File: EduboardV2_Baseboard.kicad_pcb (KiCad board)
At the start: 2 copper layers, 100 x 160 mm, 145 parts, among them IC201 STK8321, IC202 PCF8563T_5,518, IC203 W25Q128JVSIQTR, IC301 XL1509-5.0E1, IC302 SY8113BADC, IC601 STK8321, IC602 SP3485EN-L_TR, IC603 WM8782SEDS_RV_C323842, IC604 CS4344-CZZ, IC605 MCP9700AT-E_TT, SW301 1FS1T1B9M2RES-5, SW401 K2-1102SP-C4SC-04, SW402 K2-1102SP-C4SC-04, SW403 K2-1102SP-C4SC-04, SW404 K2-1102SP-C4SC-04, T401 AO3400A, T402 AO3400A, T403 AO3400A, T404 AO3400A, T405 AO3400A, X201 PCIE-52P40H, X202 32.768 kHz, X203 TF-15×15, X204 CR1220-2ZX, X301 KF2EDGR-3.81-3P, X302 USB3.1C16PFSMT, X303 CH340G, X401 ER-TFT035-6, X501 BH-00105, X502 S4B-PH-SM4-K-TB(LF)(SN), X503 USB3.1C16PFSMT, X601 KF2EDGR-3.81-3P, X602 PJ-327C-4A, X603 PJ-327C-4A, Y301 X322512MSB4SI

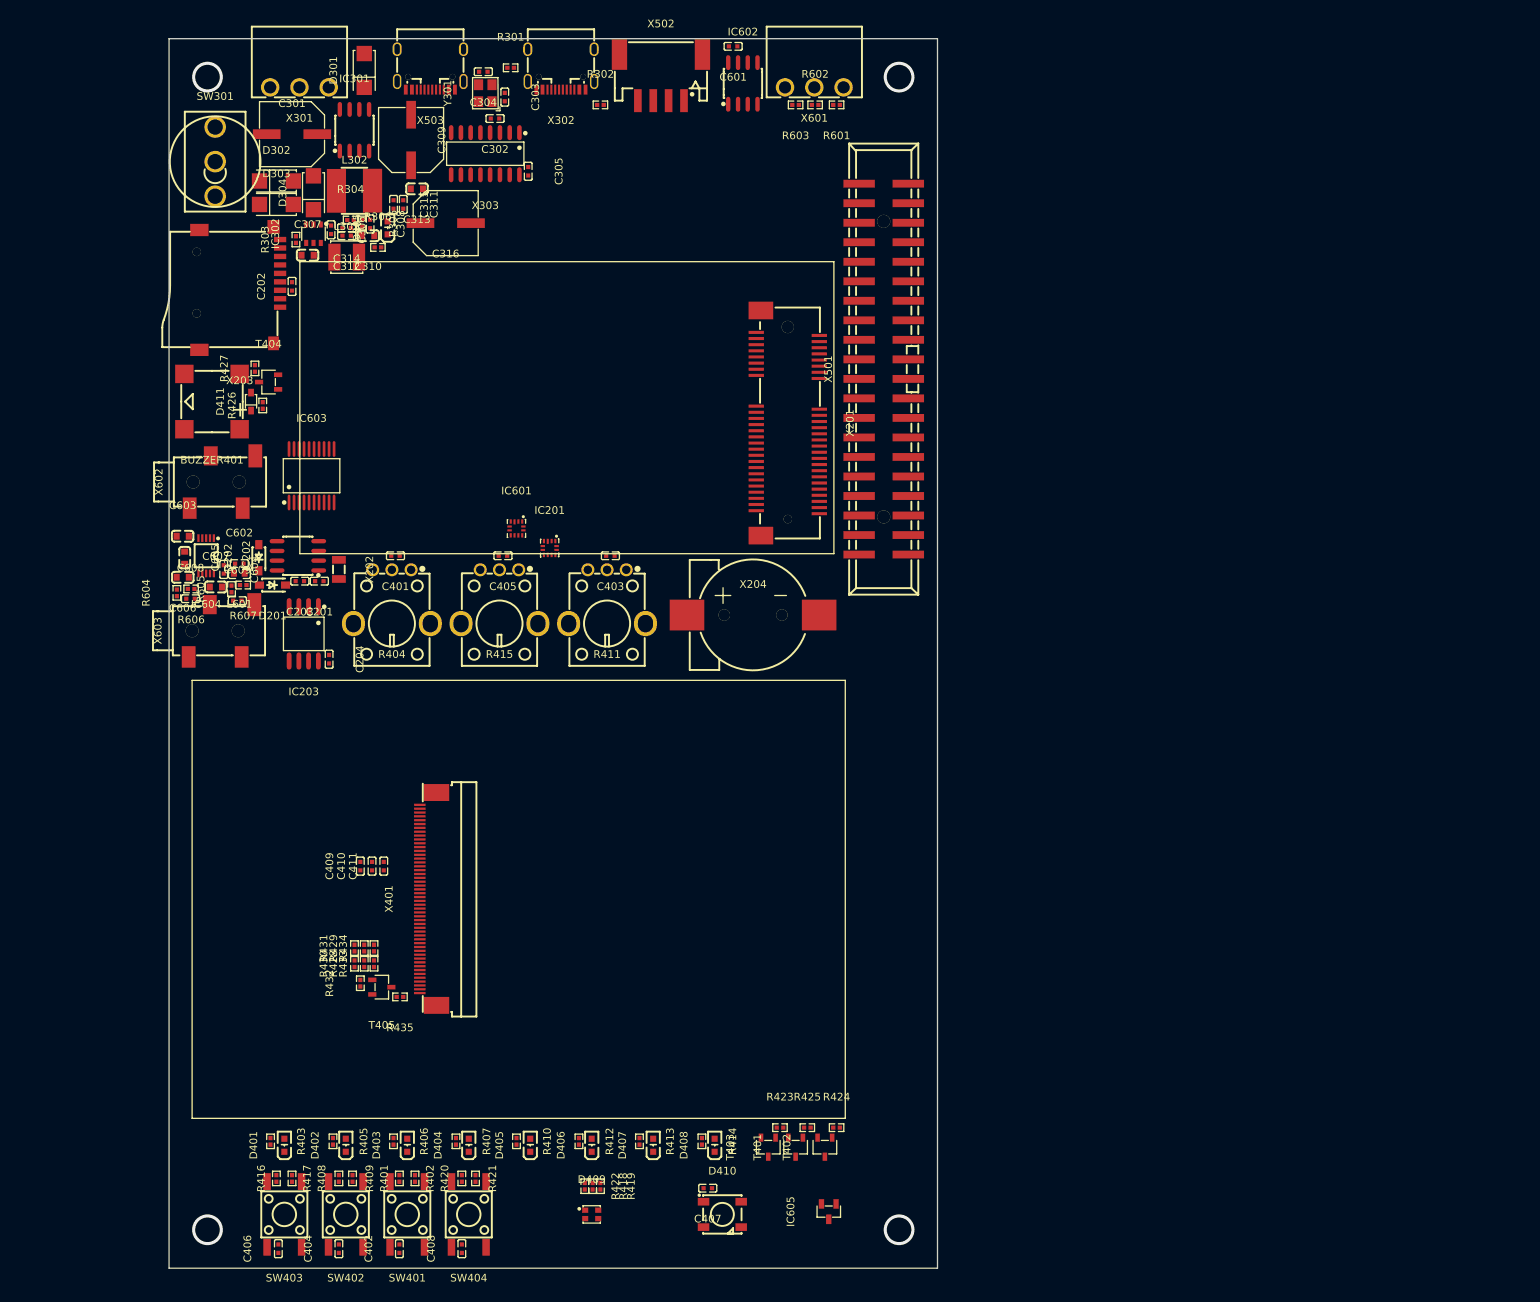
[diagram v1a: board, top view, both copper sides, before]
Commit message: reassign symbol references after page movements. Place in pcb
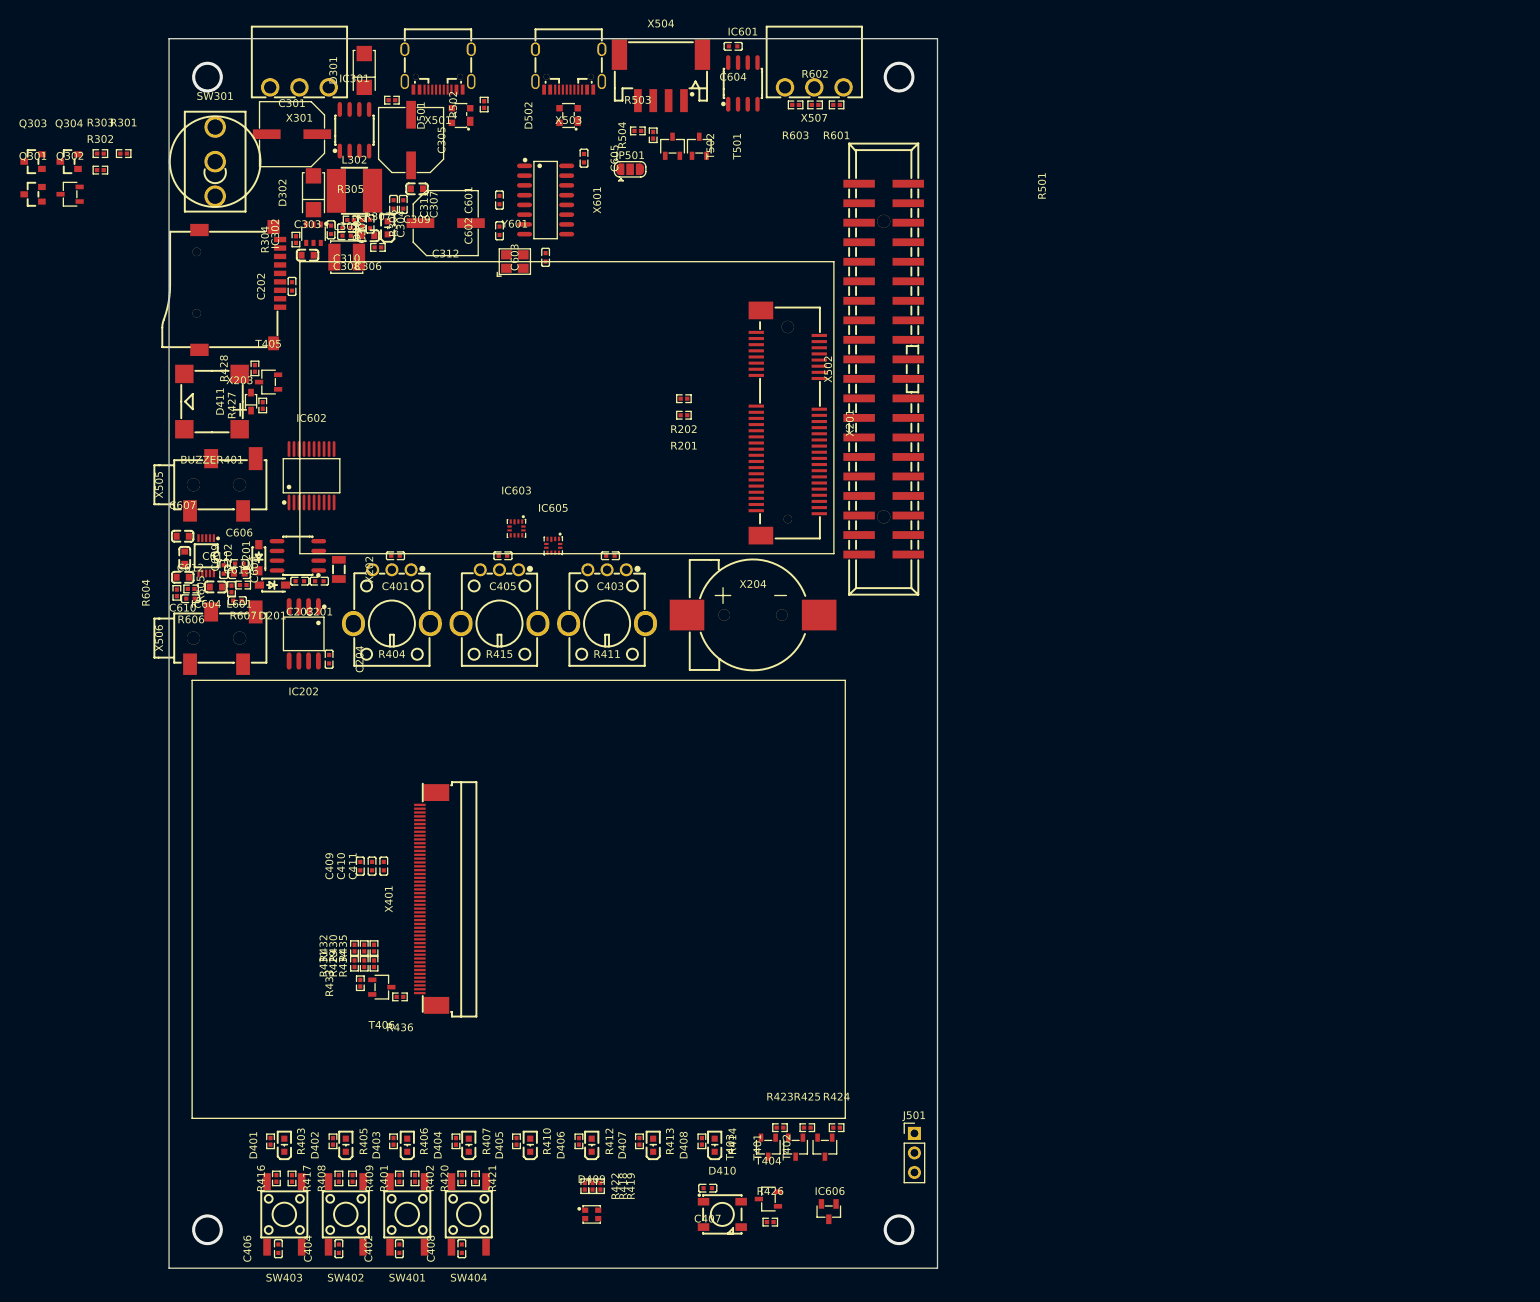
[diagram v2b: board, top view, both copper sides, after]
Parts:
- removed the C302 at (96.4, 31.4)
- removed the C303 at (97.7, 28.6)
- removed the C304 at (94.9, 25.3)
- removed the C305 at (100.7, 38.3)
- removed the D302 at (68.0, 39.5)
- removed the D303 at (68.0, 42.6)
- removed the IC201 at (103.5, 87.3)
- removed X302: USB3.1C16PFSMT, eduboardv2:USB-C-SMD_TYPE-C-USB-17
- removed X303: CH340G, eduboardv2:SOIC-16_L9.9-W3.9-P1.27-LS6.0-BL
- removed X602, X603: PJ-327C-4A, eduboardv2:AUDIO-SMD_PJ-327C-4A
- removed Y301: X322512MSB4SI, eduboardv2:OSC-SMD_4P-L3.2-W2.5-BL
- added C601: 100nF, 50V, eduboardv2:C0402, F.Cu at (97.0, 42.0)
- added C602: 22pF, eduboardv2:C0402, F.Cu at (97.0, 46.0)
- added C603: 22pF, eduboardv2:C0402, F.Cu at (103.0, 49.5)
- added C605: 100nF, 50V, eduboardv2:C0402, F.Cu at (108.0, 36.5)
- added D501: PRTR5V0U2X_C2827688, eduboardv2:SOT-143-4_L2.9-W1.3-P1.92-LS2.4-BL, F.Cu at (92.0, 31.0)
- added D502: PRTR5V0U2X_C2827688, eduboardv2:SOT-143-4_L2.9-W1.3-P1.92-LS2.4-BL, F.Cu at (106.0, 31.0)
- added IC605: STK8321, eduboardv2:LGA-12_L2.0-W2.0-P0.50-TR, F.Cu at (104.0, 87.0)
- added J501: Conn_WS2812_Extern, Connector_PinHeader_2.54mm:PinHeader_1x03_P2.54mm_Vertical, F.Cu at (151.0, 163.5)
- added JP501: Stemma Voltage Selector, Jumper:SolderJumper-3_P1.3mm_Open_RoundedPad1.0x1.5mm, F.Cu at (114.0, 38.0)
- added Q301: AO3401A, eduboardv2:SOT-23_L2.9-W1.3-P1.90-LS2.4-BR, F.Cu at (36.3, 41.2)
- added Q302: AO3400A, eduboardv2:SOT-23-3_L2.9-W1.6-P1.90-LS2.8-BR, F.Cu at (41.1, 41.2)
- added Q303: AO3401A, eduboardv2:SOT-23_L2.9-W1.3-P1.90-LS2.4-BR, F.Cu at (36.3, 37.0)
- added Q304: AO3401A, eduboardv2:SOT-23_L2.9-W1.3-P1.90-LS2.4-BR, F.Cu at (41.0, 37.0)
- added R201: 10k, eduboardv2:R0402, F.Cu at (121.0, 70.0)
- added R202: 10k, eduboardv2:R0402, F.Cu at (121.0, 67.8)
- added R303: 1M, eduboardv2:R0402, F.Cu at (45.1, 36.0)
- added R426: 10k, eduboardv2:R0402, F.Cu at (132.2, 175.0)
- added R501: 5.1k, eduboardv2:R0402, F.Cu at (83.0, 29.0)
- added R502: 5.1k, eduboardv2:R0402, F.Cu at (95.0, 29.6)
- added R503: 10k, eduboardv2:R0402, F.Cu at (115.0, 33.0)
- added R504: 10k, eduboardv2:R0402, F.Cu at (117.0, 33.6)
- added T404: AO3400A, eduboardv2:SOT-23-3_L2.9-W1.6-P1.90-LS2.8-BR, F.Cu at (132.0, 172.0)
- added T501: AO3400A, eduboardv2:SOT-23-3_L2.9-W1.6-P1.90-LS2.8-BR, F.Cu at (123.0, 35.0)
- added T502: AO3400A, eduboardv2:SOT-23-3_L2.9-W1.6-P1.90-LS2.8-BR, F.Cu at (119.5, 35.0)
- added X501: USB3.1C16PFSMT, eduboardv2:USB-C-SMD_TYPE-C-USB-17, F.Cu at (89.0, 25.0)
- added X505: PJ-327C-4A, eduboardv2:AUDIO-SMD_PJ-327C-4A, F.Cu at (61.0, 79.0)
- added X506: PJ-327C-4A, eduboardv2:AUDIO-SMD_PJ-327C-4A, F.Cu at (61.0, 99.0)
- added X507: KF2EDGR-3.81-3P, eduboardv2:CONN-TH_3P-P3.81_KF2EDGR-3.81-3P, F.Cu at (138.0, 27.3)
- added Y601: X322512MSB4SI, eduboardv2:OSC-SMD_4P-L3.2-W2.5-BL, F.Cu at (99.0, 50.0)
- R301, R302: value 5.1k -> 1M
- X601: value KF2EDGR-3.81-3P -> CH340G; footprint eduboardv2:CONN-TH_3P-P3.81_KF2EDGR-3.81-3P -> eduboardv2:SOIC-16_L9.9-W3.9-P1.27-LS6.0-BL
- moved R302 65.6 mm to (45.1, 38.1)
- moved R301 51.6 mm to (48.1, 36.0)
- moved X601 37.9 mm to (103.0, 42.0), turned to -90 degrees
- moved X503 18.0 mm to (106.0, 25.0)
- renumbered C306 to C302, C307 to C303, C308 to C304, C309 to C305, C310 to C306, C311 to C307, C312 to C308, C313 to C309, C314 to C310, C315 to C311, C316 to C312, C601 to C604, C602 to C606, C603 to C607, C604 to C608, C605 to C609, C606 to C610, C607 to C611, C608 to C612, C609 to C613, D304 to D302, D305 to D303, IC202 to IC201, IC203 to IC202, IC602 to IC601, IC603 to IC602, IC601 to IC603, IC605 to IC606, R303 to R304, R304 to R305, R305 to R306, R306 to R307, R426 to R427, R427 to R428, R428 to R429, R429 to R430, R430 to R431, R431 to R432, R432 to R433, R433 to R434, R434 to R435, R435 to R436, T404 to T405, T405 to T406, X501 to X502, X502 to X504
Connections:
- C612 pad 2: Net-(C608-Pad2) (its old number) -> AudioOutRight
- C613 pad 2: Net-(C609-Pad2) (its old number) -> AudioOutLeft
- D410 pad 2: unconnected-(D410-Pad2) -> WS2812_DOUT
- D410 pad 4: WS2812_DIN -> Net-(D410-Pad4)
- IC601 pad 6: Net-(IC602-Pad6) -> RS485_B
- IC601 pad 7: Net-(IC602-Pad7) -> RS485_A
- R302 pad 2: Net-(R302-Pad2) -> Net-(Q303-Pad2)
- R601 pad 2: Net-(IC602-Pad7) -> RS485_A
- R602 pad 1: Net-(IC602-Pad6) -> RS485_B
- R602 pad 2: Net-(IC602-Pad7) -> RS485_A
- R603 pad 1: Net-(IC602-Pad6) -> RS485_B
- R606 pad 1: Net-(C608-Pad2) (its old number) -> AudioOutRight
- R607 pad 1: Net-(C609-Pad2) (its old number) -> AudioOutLeft
- SW301 pad 1: Net-(D302-Pad1) (its old number) -> Net-(Q303-Pad2)
- X504 pad 1: unconnected-(X502-Pad1) (its old number) -> Net-(R503-Pad1)
- X504 pad 2: unconnected-(X502-Pad2) (its old number) -> Net-(R504-Pad1)
- X504 pad 3: unconnected-(X502-Pad3) (its old number) -> Net-(JP501-Pad2)
- X504 pad 4: unconnected-(X502-Pad4) (its old number) -> Net-(X504-Pad4)
- X504 pad 5: unconnected-(X502-Pad5) (its old number) -> Net-(X504-Pad5)
- X504 pad 6: unconnected-(X502-Pad6) (its old number) -> Net-(X504-Pad6)
- X601 pad 1: Net-(IC602-Pad7) -> Net-(X601-Pad1)
- X601 pad 2: Net-(X601-Pad2) -> USB_UART0_TX
- X601 pad 3: Net-(IC602-Pad6) -> USB_UART0_RX

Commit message: fix power symbol problem.
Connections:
- BUZZER401 pad 1: Net-(BUZZER401-Pad1) -> +3.3V
- C201 pad 2: Net-(C201-Pad2) -> GND
- C202 pad 1: Net-(C202-Pad1) -> GND
- C202 pad 2: Net-(C202-Pad2) -> +3.3V
- C203 pad 1: Net-(C203-Pad1) -> GND
- C204 pad 1: Net-(C204-Pad1) -> GND
- C204 pad 2: Net-(C204-Pad2) -> +3.3V
- C301 pad 1: Net-(C301-Pad1) -> V_EXT
- C301 pad 2: Net-(C301-Pad2) -> GND
- C303 pad 1: Net-(C303-Pad1) -> GND
- C303 pad 2: Net-(C303-Pad2) -> +5V
- C304 pad 2: Net-(C304-Pad2) -> +3.3V
- C305 pad 1: Net-(C305-Pad1) -> +5V_EXT
- C305 pad 2: Net-(C305-Pad2) -> GND
- C306 pad 1: Net-(C306-Pad1) -> GND
- C306 pad 2: Net-(C304-Pad2) -> +3.3V
- C307 pad 1: Net-(C305-Pad1) -> +5V_EXT
- C307 pad 2: Net-(C307-Pad2) -> GND
- C308 pad 1: Net-(C304-Pad2) -> +3.3V
- C308 pad 2: Net-(C308-Pad2) -> GND
- C309 pad 1: Net-(C309-Pad1) -> GND
- C309 pad 2: Net-(C305-Pad1) -> +5V_EXT
- C310 pad 1: Net-(C304-Pad2) -> +3.3V
- C310 pad 2: Net-(C310-Pad2) -> GND
- C311 pad 1: Net-(C305-Pad1) -> +5V_EXT
- C311 pad 2: Net-(C311-Pad2) -> GND
- C312 pad 1: Net-(C304-Pad2) -> +3.3V
- C312 pad 2: Net-(C312-Pad2) -> GND
- C401 pad 1: Net-(C401-Pad1) -> GND
- C402 pad 1: Net-(C402-Pad1) -> GND
- C403 pad 1: Net-(C403-Pad1) -> GND
- C404 pad 1: Net-(C404-Pad1) -> GND
- C405 pad 1: Net-(C405-Pad1) -> GND
- C406 pad 1: Net-(C406-Pad1) -> GND
- C407 pad 1: Net-(C407-Pad1) -> GND
- C407 pad 2: Net-(C407-Pad2) -> +5V
- C408 pad 1: Net-(C408-Pad1) -> GND
- C409 pad 1: Net-(C409-Pad1) -> GND
- C409 pad 2: Net-(C409-Pad2) -> +3.3V
- C410 pad 1: Net-(C409-Pad1) -> GND
- C410 pad 2: Net-(C409-Pad2) -> +3.3V
- C411 pad 1: Net-(C409-Pad1) -> GND
- C411 pad 2: Net-(C409-Pad2) -> +3.3V
- C601 pad 1: Net-(C601-Pad1) -> GND
- C602 pad 1: Net-(C602-Pad1) -> GND
- C603 pad 1: Net-(C603-Pad1) -> GND
- C604 pad 1: Net-(C604-Pad1) -> GND
- C604 pad 2: Net-(C604-Pad2) -> +3.3V
- C605 pad 1: Net-(C605-Pad1) -> GND
- C605 pad 2: Net-(C605-Pad2) -> V_USB
- C606 pad 1: Net-(C606-Pad1) -> GND
- C606 pad 2: Net-(C606-Pad2) -> +3.3V
- C607 pad 1: Net-(C607-Pad1) -> GND
- C608 pad 1: Net-(C608-Pad1) -> GND
- C609 pad 1: Net-(C609-Pad1) -> GND
- C612 pad 1: Net-(C612-Pad1) -> GND
- C613 pad 1: Net-(C613-Pad1) -> GND
- D201 pad 2: Net-(D201-Pad2) -> +3.3V
- D301 pad 1: Net-(C301-Pad1) -> V_EXT
- D301 pad 2: Net-(D301-Pad2) -> GND
- D302 pad 2: Net-(D302-Pad2) -> GND
- D303 pad 1: Net-(C304-Pad2) -> +3.3V
- D401 pad 2: Net-(D401-Pad2) -> GND
- D402 pad 2: Net-(D402-Pad2) -> GND
- D403 pad 2: Net-(D403-Pad2) -> GND
- D404 pad 2: Net-(D404-Pad2) -> GND
- D405 pad 2: Net-(D405-Pad2) -> GND
- D406 pad 2: Net-(D406-Pad2) -> GND
- D407 pad 2: Net-(D407-Pad2) -> GND
- D408 pad 2: Net-(D408-Pad2) -> GND
- D409 pad 3: Net-(D409-Pad3) -> +3.3V
- D410 pad 1: Net-(C407-Pad2) -> +5V
- D410 pad 3: Net-(D410-Pad3) -> GND
- D411 pad 1: Net-(BUZZER401-Pad1) -> +3.3V
- D501 pad 1: Net-(D501-Pad1) -> GND
- D501 pad 4: Net-(D501-Pad4) -> V_USB
- D502 pad 1: Net-(D502-Pad1) -> GND
- D502 pad 4: Net-(D502-Pad4) -> +5V
- IC201 pad 4: Net-(IC201-Pad4) -> GND
- IC202 pad 4: Net-(IC202-Pad4) -> GND
- IC202 pad 8: Net-(C204-Pad2) -> +3.3V
- IC301 pad 1: Net-(IC301-Pad1) -> V_EXT
- IC301 pad 3: Net-(C305-Pad1) -> +5V_EXT
- IC301 pad 5: Net-(IC301-Pad5) -> GND
- IC301 pad 6: Net-(IC301-Pad5) -> GND
- IC301 pad 7: Net-(IC301-Pad5) -> GND
- IC301 pad 8: Net-(IC301-Pad5) -> GND
- IC302 pad 2: Net-(IC302-Pad2) -> GND
- IC302 pad 5: Net-(C303-Pad2) -> +5V
- IC601 pad 5: Net-(IC601-Pad5) -> GND
- IC601 pad 8: Net-(C604-Pad2) -> +3.3V
- IC604 pad 8: Net-(IC604-Pad8) -> GND
- J501 pad 1: Net-(J501-Pad1) -> +5V
- J501 pad 3: Net-(J501-Pad3) -> GND
- JP501 pad 1: Net-(JP501-Pad1) -> +3.3V
- JP501 pad 3: Net-(JP501-Pad3) -> +5V
- L301 pad 2: Net-(C304-Pad2) -> +3.3V
- L302 pad 2: Net-(C305-Pad1) -> +5V_EXT
- L601 pad 1: Net-(C606-Pad2) -> +3.3V
- Q301 pad 1: Net-(Q301-Pad1) -> GND
- Q301 pad 3: Net-(Q301-Pad3) -> +5V_EXT
- Q302 pad 2: Net-(Q302-Pad2) -> GND
- Q304 pad 3: Net-(Q304-Pad3) -> V_USB
- R201 pad 2: Net-(R201-Pad2) -> +3.3V
- R202 pad 2: Net-(R202-Pad2) -> +3.3V
- R301 pad 1: Net-(R301-Pad1) -> GND
- R303 pad 1: Net-(R303-Pad1) -> GND
- R303 pad 2: Net-(Q304-Pad3) -> V_USB
- R304 pad 2: Net-(C303-Pad2) -> +5V
- R305 pad 1: Net-(R305-Pad1) -> GND
- R306 pad 2: Net-(C304-Pad2) -> +3.3V
- R307 pad 1: Net-(R307-Pad1) -> GND
- R401 pad 2: Net-(R401-Pad2) -> +3.3V
- R402 pad 1: Net-(R402-Pad1) -> GND
- R404 pad 1: Net-(R404-Pad1) -> GND
- R404 pad 3: Net-(R404-Pad3) -> +3.3V
- R408 pad 2: Net-(R408-Pad2) -> +3.3V
- R409 pad 1: Net-(R409-Pad1) -> GND
- R411 pad 1: Net-(R411-Pad1) -> GND
- R411 pad 3: Net-(R411-Pad3) -> +3.3V
- R415 pad 1: Net-(R415-Pad1) -> GND
- R415 pad 3: Net-(R415-Pad3) -> +3.3V
- R416 pad 2: Net-(R416-Pad2) -> +3.3V
- R417 pad 1: Net-(R417-Pad1) -> GND
- R420 pad 2: Net-(R420-Pad2) -> +3.3V
- R421 pad 1: Net-(R421-Pad1) -> GND
- R426 pad 2: Net-(R426-Pad2) -> +5V
- R429 pad 1: Net-(R429-Pad1) -> +3.3V
- R430 pad 2: Net-(R430-Pad2) -> GND
- R431 pad 1: Net-(R429-Pad1) -> +3.3V
- R432 pad 2: Net-(R430-Pad2) -> GND
- R434 pad 1: Net-(R429-Pad1) -> +3.3V
- R435 pad 2: Net-(R430-Pad2) -> GND
- R436 pad 2: Net-(R436-Pad2) -> +3.3V
- R501 pad 2: Net-(R501-Pad2) -> GND
- R502 pad 1: Net-(R502-Pad1) -> GND
- R502 pad 2: Net-(R502-Pad2) -> V_USB
- R601 pad 1: Net-(R601-Pad1) -> GND
- R603 pad 2: Net-(R603-Pad2) -> +3.3V
- R604 pad 1: Net-(R604-Pad1) -> GND
- R605 pad 1: Net-(R605-Pad1) -> GND
- SW301 pad 2: Net-(SW301-Pad2) -> +5V
- SW301 pad 3: Net-(SW301-Pad2) -> +5V
- T401 pad 2: Net-(T401-Pad2) -> GND
- T402 pad 2: Net-(T402-Pad2) -> GND
- T403 pad 2: Net-(T403-Pad2) -> GND
- T404 pad 1: Net-(T404-Pad1) -> +3.3V
- T405 pad 2: Net-(T405-Pad2) -> GND
- T406 pad 2: Net-(T406-Pad2) -> GND
- T501 pad 1: Net-(T501-Pad1) -> +3.3V
- T502 pad 1: Net-(T502-Pad1) -> +3.3V
- X203 pad 4: Net-(C202-Pad2) -> +3.3V
- X203 pad 6: Net-(X203-Pad6) -> GND
- X204 pad 2: Net-(X204-Pad2) -> GND
- X301 pad 1: Net-(C301-Pad1) -> V_EXT
- X301 pad 3: Net-(D301-Pad2) -> GND
- X401 pad 11: Net-(X401-Pad11) -> GND
- X401 pad 12: Net-(X401-Pad11) -> GND
- X401 pad 13: Net-(X401-Pad13) -> +3.3V
- X401 pad 14: Net-(X401-Pad14) -> GND
- X401 pad 15: Net-(X401-Pad14) -> GND
- X401 pad 16: Net-(X401-Pad14) -> GND
- X401 pad 17: Net-(X401-Pad14) -> GND
- X401 pad 18: Net-(X401-Pad14) -> GND
- X401 pad 19: Net-(X401-Pad14) -> GND
- X401 pad 20: Net-(X401-Pad14) -> GND
- X401 pad 21: Net-(X401-Pad14) -> GND
- X401 pad 22: Net-(X401-Pad14) -> GND
- X401 pad 23: Net-(X401-Pad14) -> GND
- X401 pad 24: Net-(X401-Pad14) -> GND
- X401 pad 25: Net-(X401-Pad14) -> GND
- X401 pad 26: Net-(X401-Pad14) -> GND
- X401 pad 27: Net-(X401-Pad14) -> GND
- X401 pad 28: Net-(X401-Pad14) -> GND
- X401 pad 29: Net-(X401-Pad14) -> GND
- X401 pad 30: Net-(X401-Pad14) -> GND
- X401 pad 31: Net-(X401-Pad14) -> GND
- X401 pad 32: Net-(X401-Pad14) -> GND
- X401 pad 35: Net-(X401-Pad35) -> +3.3V
- X401 pad 40: Net-(X401-Pad40) -> +3.3V
- X401 pad 41: Net-(X401-Pad40) -> +3.3V
- X401 pad 42: Net-(X401-Pad40) -> +3.3V
- X401 pad 43: Net-(X401-Pad43) -> GND
- X401 pad 48: Net-(X401-Pad48) -> GND
- X401 pad 49: Net-(X401-Pad48) -> GND
- X401 pad 50: Net-(X401-Pad48) -> GND
- X501 pad 0: Net-(X501-Pad0) -> GND
- X501 pad A1: Net-(X501-PadA1) -> GND
- X501 pad A12: Net-(X501-PadA12) -> GND
- X501 pad A4: Net-(R502-Pad2) -> V_USB
- X501 pad A5: Net-(R502-Pad2) -> V_USB
- X501 pad A9: Net-(R502-Pad2) -> V_USB
- X503 pad 0: Net-(X503-Pad0) -> GND
- X503 pad A1: Net-(X503-PadA1) -> GND
- X503 pad A12: Net-(X503-PadA12) -> GND
- X504 pad 4: Net-(X504-Pad4) -> GND
- X504 pad 5: Net-(X504-Pad5) -> GND
- X504 pad 6: Net-(X504-Pad6) -> GND
- X505 pad 1: Net-(X505-Pad1) -> GND
- X506 pad 1: Net-(X506-Pad1) -> GND
- X507 pad 2: Net-(X507-Pad2) -> GND
- X601 pad 1: Net-(X601-Pad1) -> GND
- X601 pad 16: Net-(C605-Pad2) -> V_USB
- Y601 pad 2: Net-(Y601-Pad2) -> GND
- Y601 pad 4: Net-(Y601-Pad4) -> GND
